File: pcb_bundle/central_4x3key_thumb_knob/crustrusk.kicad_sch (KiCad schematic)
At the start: 54 parts, among them J1 AudioJack4, J2 AudioJack4, P1 Conn_01x06_Socket

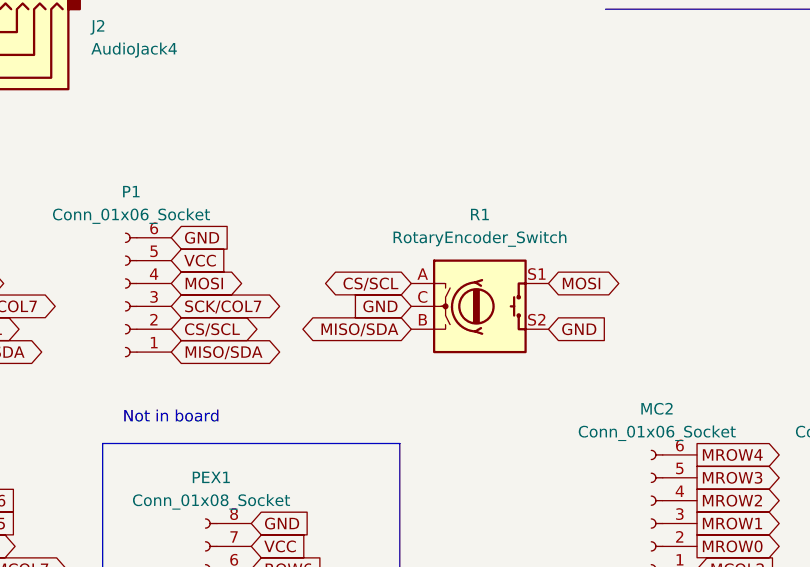
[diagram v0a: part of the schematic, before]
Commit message: changed mainboard jst socket direction, added mousebite
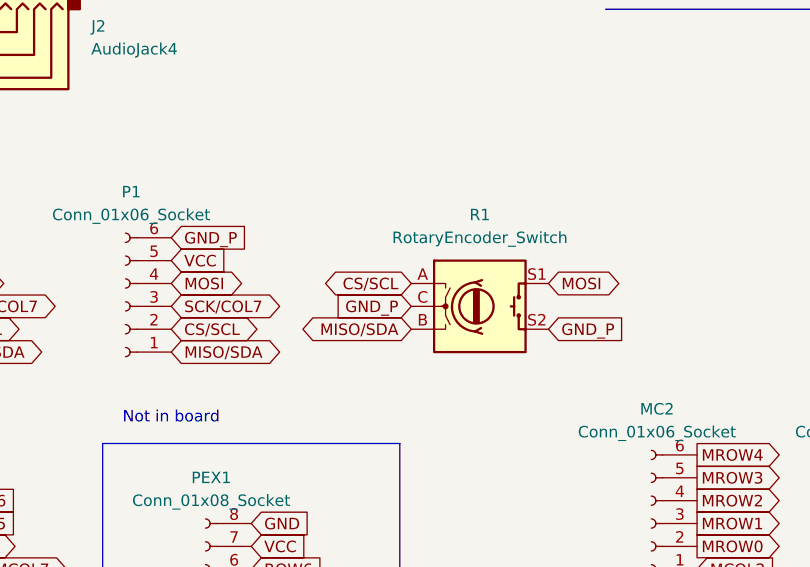
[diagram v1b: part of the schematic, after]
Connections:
- net GND: no longer P1.6 (Pin_6), R1.C, R1.S2
- new net GND_P: P1.6 (Pin_6), R1.C, R1.S2
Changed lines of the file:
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@@
 		)
 	)
-	(global_label "GND"
+	(global_label "GND_P"
 		(shape input)
 		(at 92.71 114.3 180)
@@
 		)
 		(property "Intersheetrefs" "${INTERSHEET_REFS}"
-			(at 85.8543 114.3 0)
+			(at 83.6167 114.3 0)
 			(hide yes)
 			(show_name no)
@@
 		)
 	)
-	(global_label "GND"
+	(global_label "GND_P"
 		(shape input)
 		(at 107.95 116.84 0)
@@
 		)
 		(property "Intersheetrefs" "${INTERSHEET_REFS}"
-			(at 114.8057 116.84 0)
+			(at 117.0433 116.84 0)
 			(hide yes)
 			(show_name no)
@@
 		)
 	)
-	(global_label "GND"
+	(global_label "GND_P"
 		(shape input)
 		(at 66.04 106.68 0)
@@
 		)
 		(property "Intersheetrefs" "${INTERSHEET_REFS}"
-			(at 72.8957 106.68 0)
-			(hide yes)
-			(show_name no)
+			(at 75.1333 106.68 0)
+			(hide yes)
+			(show_name no)
